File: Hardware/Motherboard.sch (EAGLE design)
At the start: 67 parts, among them J1 MICROMOD-2222-C, J10 MICRO-SD-PUSH-PUSH-EXT-PIN, J2 Vertical Qwiic Connector, J4 QWIIC_RIGHT_ANGLE, J5 CORTEX_JTAG_DEBUG_MINIMUM_PTH, J6 MICROMOD_CARRIER, J7 MICROMOD_CARRIER, Q1 3.1A/30V/105mΩ, U2 MCP73831, U5 AP7361C-33

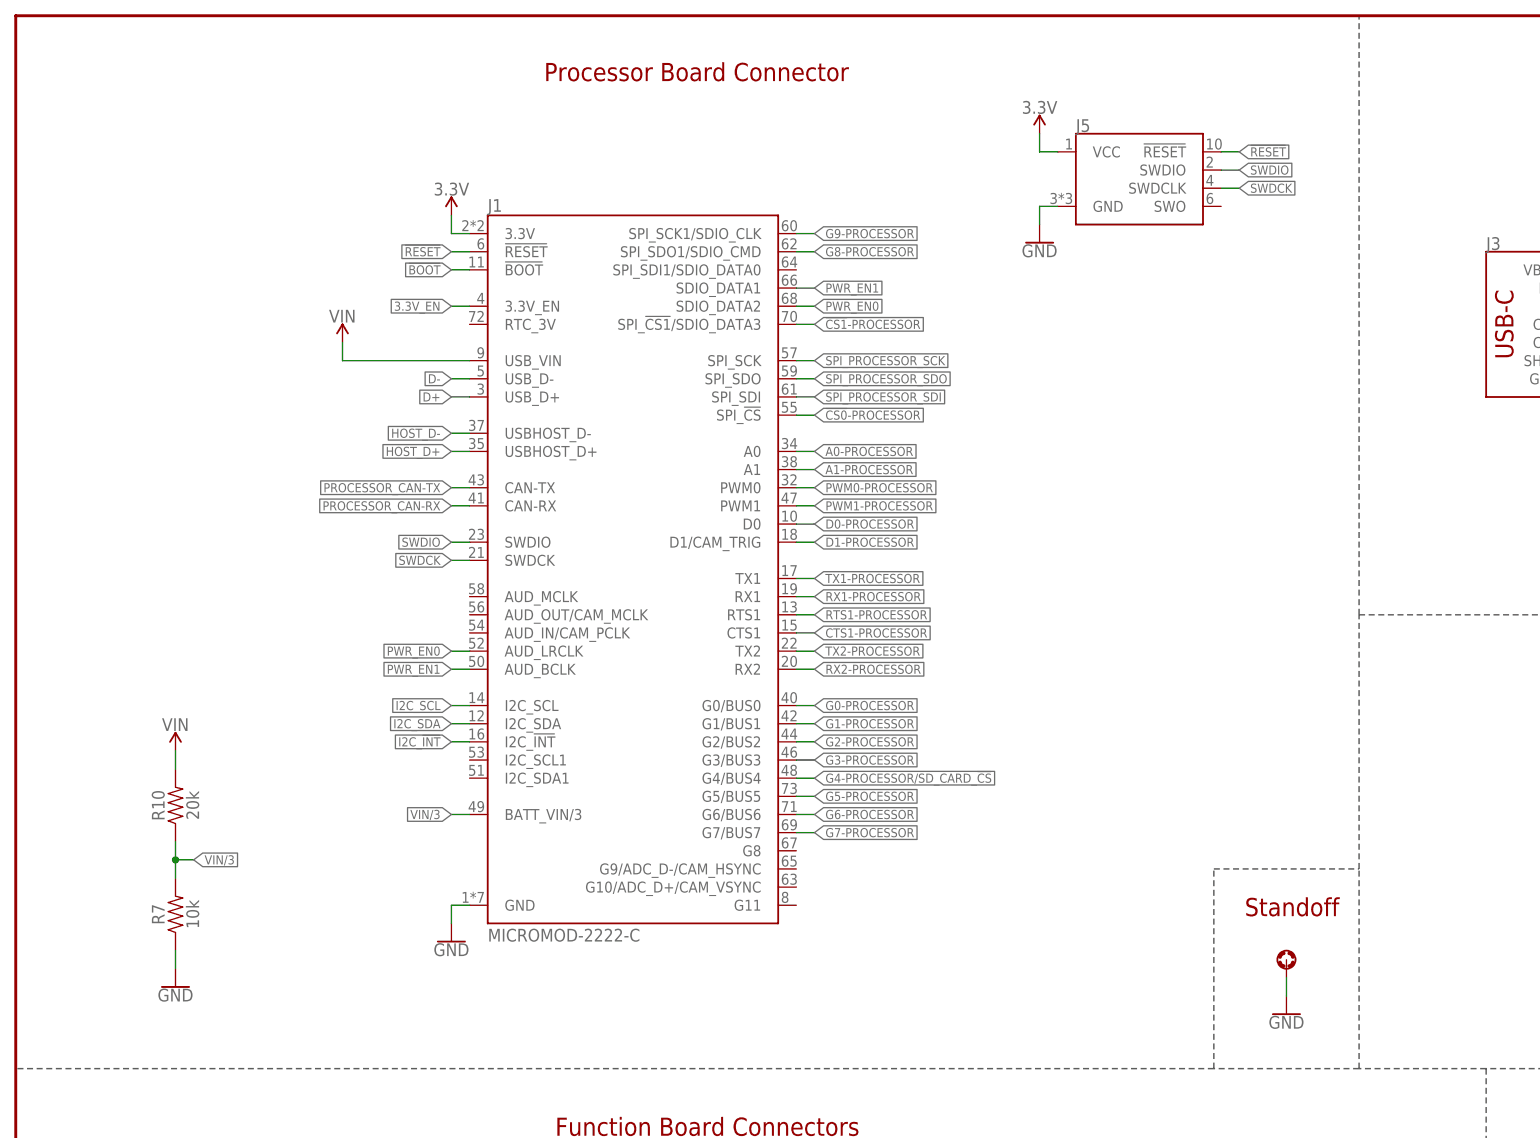
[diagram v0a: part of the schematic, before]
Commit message: Adds jumpers to route power enable pins to G0/G1 for processors that don't have those nets routed
* Adds silk to added jumpers
* Adds PROD-ID to function board connectors
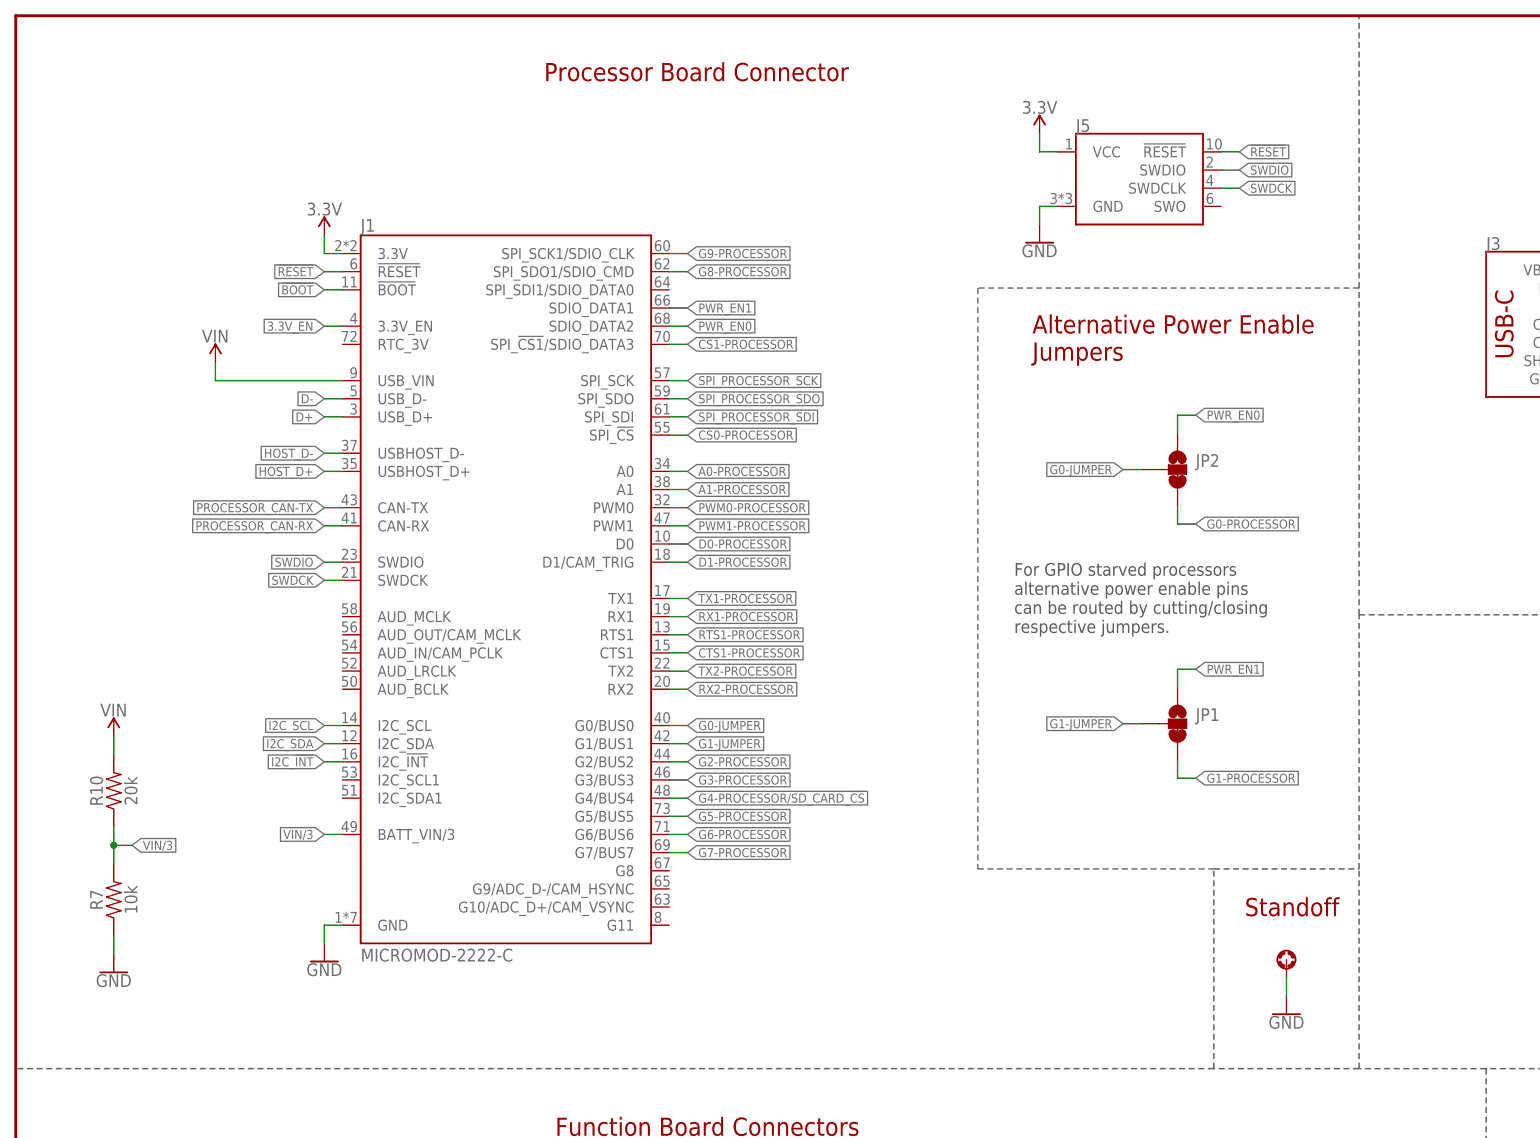
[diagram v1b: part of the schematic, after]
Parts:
- added JP1, JP2: JUMPER-SMT_3_1-NC_TRACE_SILK, SparkFun-Jumpers:JUMPER-SMT_3_1-NC_TRACE_SILK
- H2, H3, H4, H8: value STAND-OFF-REFLOW2.5MM_TALL -> STAND-OFF-REFLOW-M2.5_2.5MM_TALL; device SparkFun-Hardware:STAND-OFF-REFLOW2.5MM_TALL -> SparkFun-Hardware:STAND-OFF-REFLOW-M2.5_2.5MM_TALL
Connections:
- new net G0-JUMPER: J1.G0/BUS0, JP2.2
- new net G1-JUMPER: J1.G1/BUS1, JP1.2
- net G0-PROCESSOR: now also JP2.3; no longer J1.G0/BUS0
- net G1-PROCESSOR: now also JP1.3; no longer J1.G1/BUS1
- net PWR_EN0: now also JP2.1; no longer J1.AUD_LRCLK
- net PWR_EN1: now also JP1.1; no longer J1.AUD_BCLK
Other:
- note added: "Alternative Power Enable Jumpers"
- note added: "For GPIO starved processors alternative power enable pins can be routed by cutting/closing respective jumpers."
- moved on the sheet: J1, R10, R7

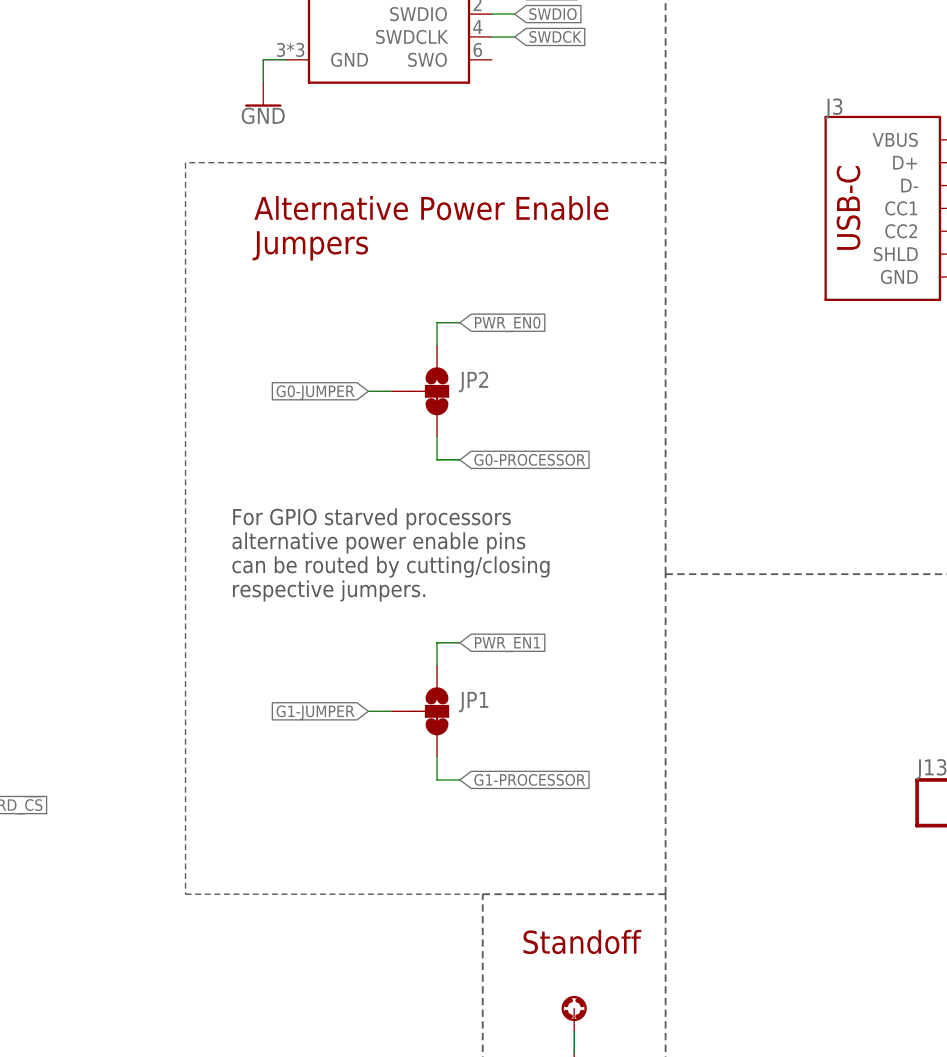
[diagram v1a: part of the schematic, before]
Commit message: Adds PTH headers for shunt selectable settings on G0 and G1 for PWR_EN0 and PWR_EN1 respectively
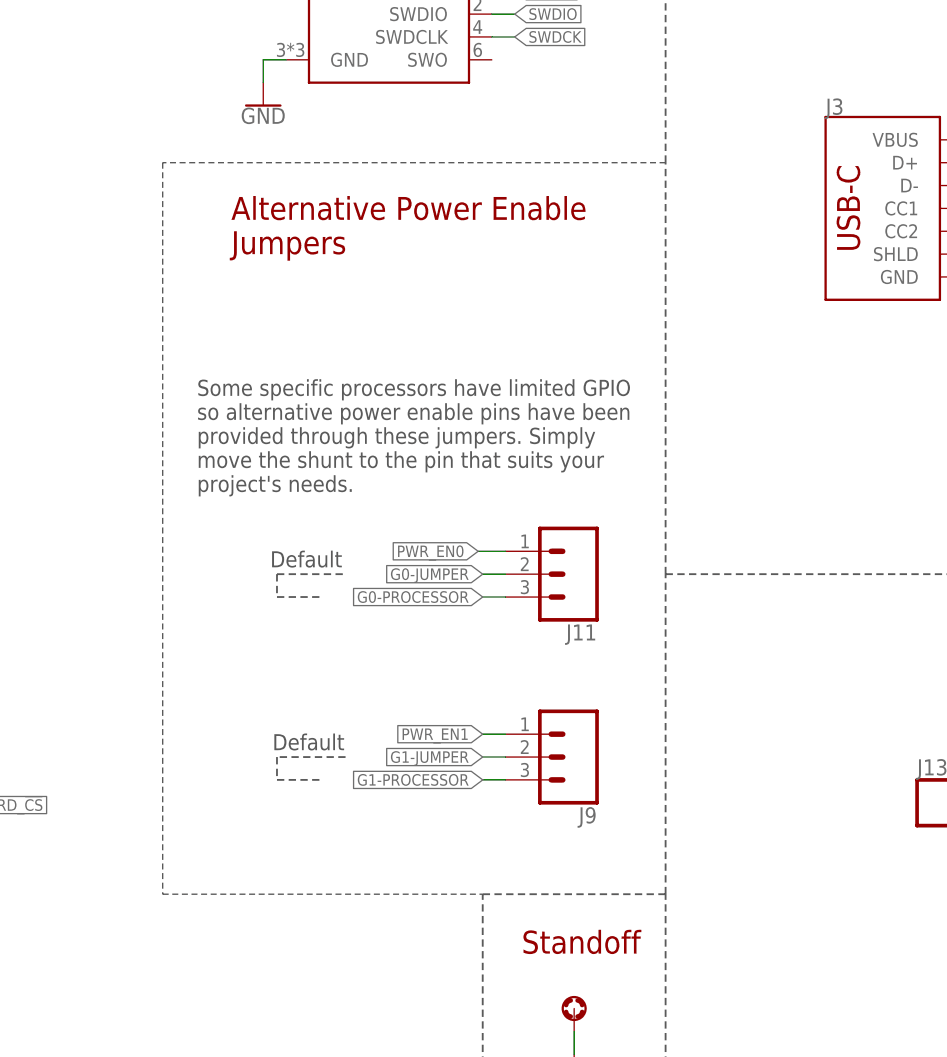
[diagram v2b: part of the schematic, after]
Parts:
- removed JP1, JP2: JUMPER-SMT_3_1-NC_TRACE_SILK, SparkFun-Jumpers:JUMPER-SMT_3_1-NC_TRACE_SILK
- added J11, J9: (no value), SparkFun-Connectors:CONN_03LOCK
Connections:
- net G0-JUMPER: now also J11.2; no longer JP2.2
- net G0-PROCESSOR: now also J11.3; no longer JP2.3
- net G1-JUMPER: now also J9.2; no longer JP1.2
- net G1-PROCESSOR: now also J9.3; no longer JP1.3
- net PWR_EN0: now also J11.1; no longer JP2.1
- net PWR_EN1: now also J9.1; no longer JP1.1
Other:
- note added: "Default"
- note added: "Some specific processors have limited GPIO so alternative power enable pins have been provided through these jumpers. Simply move the shunt to the pin that suits your project's needs."
- note removed: "For GPIO starved processors alternative power enable pins can be routed by cutting/closing respective jumpers."
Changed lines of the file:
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@@
 <part name="R6" library="SparkFun-Resistors" deviceset="10KOHM" device="-0603-1/10W-1%" value="10k"/>
 <part name="GND8" library="SparkFun-PowerSymbols" deviceset="GND" device=""/>
-<part name="JP1" library="SparkFun-Jumpers" deviceset="JUMPER-SMT_3_1-NC_TRACE" device="_SILK" package3d_urn="urn:adsk.eagle:package:39288/1"/>
-<part name="JP2" library="SparkFun-Jumpers" deviceset="JUMPER-SMT_3_1-NC_TRACE" device="_SILK" package3d_urn="urn:adsk.eagle:package:39288/1"/>
+<part name="J9" library="SparkFun-Connectors" deviceset="CONN_03" device="LOCK"/>
+<part name="J11" library="SparkFun-Connectors" deviceset="CONN_03" device="LOCK"/>
 </parts>
 <sheets>
@@
 <text x="171.958" y="153.416" size="2.54" layer="94" font="vector">Standoff</text>
 <text x="187.96" y="22.86" size="2.54" layer="94" font="vector">Standoff</text>
-<wire x1="187.96" y1="241.3" x2="134.62" y2="241.3" width="0.1524" layer="97" style="longdash"/>
-<wire x1="134.62" y1="241.3" x2="134.62" y2="160.02" width="0.1524" layer="97" style="longdash"/>
-<wire x1="134.62" y1="160.02" x2="167.64" y2="160.02" width="0.1524" layer="97" style="longdash"/>
-<text x="142.24" y="231.14" size="2.54" layer="94" font="vector">Alternative Power Enable
+<wire x1="187.96" y1="241.3" x2="132.08" y2="241.3" width="0.1524" layer="97" style="longdash"/>
+<wire x1="132.08" y1="241.3" x2="132.08" y2="160.02" width="0.1524" layer="97" style="longdash"/>
+<wire x1="132.08" y1="160.02" x2="167.64" y2="160.02" width="0.1524" layer="97" style="longdash"/>
+<text x="139.7" y="231.14" size="2.54" layer="94" font="vector">Alternative Power Enable
 Jumpers</text>
-<text x="139.7" y="193.04" size="1.778" layer="97" font="vector">For GPIO starved processors
-alternative power enable pins
-can be routed by cutting/closing
-respective jumpers.</text>
+<text x="135.89" y="204.724" size="1.778" layer="97" font="vector">Some specific processors have limited GPIO
+so alternative power enable pins have been
+provided through these jumpers. Simply
+move the shunt to the pin that suits your
+project's needs.
+</text>
+<wire x1="144.78" y1="195.58" x2="144.78" y2="193.04" width="0.2032" layer="97" style="dashdot"/>
+<wire x1="144.78" y1="193.04" x2="149.86" y2="193.04" width="0.2032" layer="97" style="dashdot"/>
+<wire x1="144.78" y1="195.58" x2="152.4" y2="195.58" width="0.2032" layer="97" style="dashdot"/>
+<wire x1="152.4" y1="175.26" x2="144.78" y2="175.26" width="0.2032" layer="97" style="dashdot"/>
+<wire x1="144.78" y1="175.26" x2="144.78" y2="172.72" width="0.2032" layer="97" style="dashdot"/>
+<wire x1="144.78" y1="172.72" x2="149.86" y2="172.72" width="0.2032" layer="97" style="dashdot"/>
+<text x="144.272" y="176.022" size="1.778" layer="97" font="vector">Default</text>
+<text x="144.018" y="196.342" size="1.778" layer="97" font="vector">Default</text>
 </plain>
 <instances>
@@
 <attribute name="VALUE" x="264.16" y="218.186" size="1.778" layer="96" font="vector" align="top-center"/>
 </instance>
-<instance part="JP1" gate="G$1" x="162.56" y="180.34" smashed="yes">
-<attribute name="NAME" x="165.1" y="180.721" size="1.778" layer="95" font="vector"/>
-</instance>
-<instance part="JP2" gate="G$1" x="162.56" y="215.9" smashed="yes">
-<attribute name="NAME" x="165.1" y="216.281" size="1.778" layer="95" font="vector"/>
+<instance part="J9" gate="J$1" x="177.8" y="175.26" smashed="yes" rot="R180">
+<attribute name="VALUE" x="180.34" y="182.626" size="1.778" layer="96" font="vector" rot="R180"/>
+<attribute name="NAME" x="180.34" y="169.672" size="1.778" layer="95" font="vector" rot="R180"/>
+</instance>
+<instance part="J11" gate="J$1" x="177.8" y="195.58" smashed="yes" rot="R180">
+<attribute name="VALUE" x="180.34" y="202.946" size="1.778" layer="96" font="vector" rot="R180"/>
+<attribute name="NAME" x="180.34" y="189.992" size="1.778" layer="95" font="vector" rot="R180"/>
 </instance>
 </instances>
@@
 </segment>
 <segment>
-<pinref part="JP2" gate="G$1" pin="1"/>
-<wire x1="162.56" y1="220.98" x2="162.56" y2="223.52" width="0.1524" layer="91"/>
-<wire x1="162.56" y1="223.52" x2="165.1" y2="223.52" width="0.1524" layer="91"/>
-<label x="165.1" y="223.52" size="1.27" layer="95" font="vector" xref="yes"/>
+<label x="167.132" y="198.12" size="1.27" layer="95" font="vector" rot="R180" xref="yes"/>
+<pinref part="J11" gate="J$1" pin="1"/>
+<wire x1="170.18" y1="198.12" x2="167.132" y2="198.12" width="0.1524" layer="91"/>
 </segment>
 </net>
@@
 </segment>
 <segment>
-<pinref part="JP1" gate="G$1" pin="1"/>
-<wire x1="162.56" y1="185.42" x2="162.56" y2="187.96" width="0.1524" layer="91"/>
-<wire x1="162.56" y1="187.96" x2="165.1" y2="187.96" width="0.1524" layer="91"/>
-<label x="165.1" y="187.96" size="1.27" layer="95" font="vector" xref="yes"/>
+<label x="167.64" y="177.8" size="1.27" layer="95" font="vector" rot="R180" xref="yes"/>
+<pinref part="J9" gate="J$1" pin="1"/>
+<wire x1="170.18" y1="177.8" x2="167.64" y2="177.8" width="0.1524" layer="91"/>
 </segment>
 </net>
@@
 </segment>
 <segment>
-<pinref part="JP2" gate="G$1" pin="3"/>
-<wire x1="162.56" y1="210.82" x2="162.56" y2="208.28" width="0.1524" layer="91"/>
-<wire x1="162.56" y1="208.28" x2="165.1" y2="208.28" width="0.1524" layer="91"/>
-<label x="165.1" y="208.28" size="1.27" layer="95" font="vector" xref="yes"/>
+<label x="167.64" y="193.04" size="1.27" layer="95" font="vector" rot="R180" xref="yes"/>
+<pinref part="J11" gate="J$1" pin="3"/>
+<wire x1="170.18" y1="193.04" x2="167.64" y2="193.04" width="0.1524" layer="91"/>
 </segment>
 </net>
@@
 </segment>
 <segment>
-<pinref part="JP1" gate="G$1" pin="3"/>
-<wire x1="162.56" y1="175.26" x2="162.56" y2="172.72" width="0.1524" layer="91"/>
-<wire x1="162.56" y1="172.72" x2="165.1" y2="172.72" width="0.1524" layer="91"/>
-<label x="165.1" y="172.72" size="1.27" layer="95" font="vector" xref="yes"/>
+<label x="167.64" y="172.72" size="1.27" layer="95" font="vector" rot="R180" xref="yes"/>
+<pinref part="J9" gate="J$1" pin="3"/>
+<wire x1="170.18" y1="172.72" x2="167.64" y2="172.72" width="0.1524" layer="91"/>
 </segment>
 </net>
@@
 <net name="G1-JUMPER" class="0">
 <segment>
-<pinref part="JP1" gate="G$1" pin="2"/>
-<wire x1="157.48" y1="180.34" x2="154.94" y2="180.34" width="0.1524" layer="91"/>
-<label x="154.94" y="180.34" size="1.27" layer="95" font="vector" rot="R180" xref="yes"/>
+<label x="167.64" y="175.26" size="1.27" layer="95" font="vector" rot="R180" xref="yes"/>
+<pinref part="J9" gate="J$1" pin="2"/>
+<wire x1="170.18" y1="175.26" x2="167.64" y2="175.26" width="0.1524" layer="91"/>
 </segment>
 <segment>
@@
 <net name="G0-JUMPER" class="0">
 <segment>
-<pinref part="JP2" gate="G$1" pin="2"/>
-<wire x1="157.48" y1="215.9" x2="154.94" y2="215.9" width="0.1524" layer="91"/>
-<label x="154.94" y="215.9" size="1.27" layer="95" font="vector" rot="R180" xref="yes"/>
-</segment>
-<segment>
+<label x="167.64" y="195.58" size="1.27" layer="95" font="vector" rot="R180" xref="yes"/>
+<pinref part="J11" gate="J$1" pin="2"/>
+<wire x1="167.64" y1="195.58" x2="170.18" y2="195.58" width="0.1524" layer="91"/>
+</segment>
+<segment>
